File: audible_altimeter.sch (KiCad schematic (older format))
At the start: 0 parts

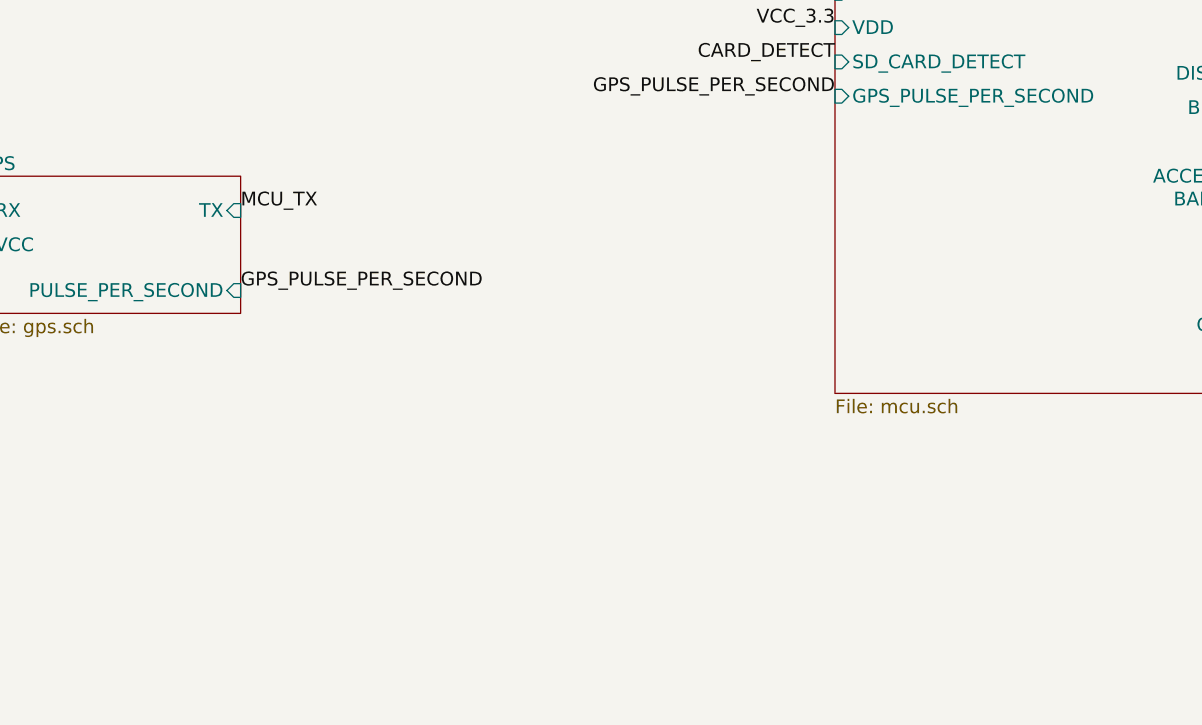
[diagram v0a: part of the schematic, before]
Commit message: Add buttons. Fix DRC. Add antenna
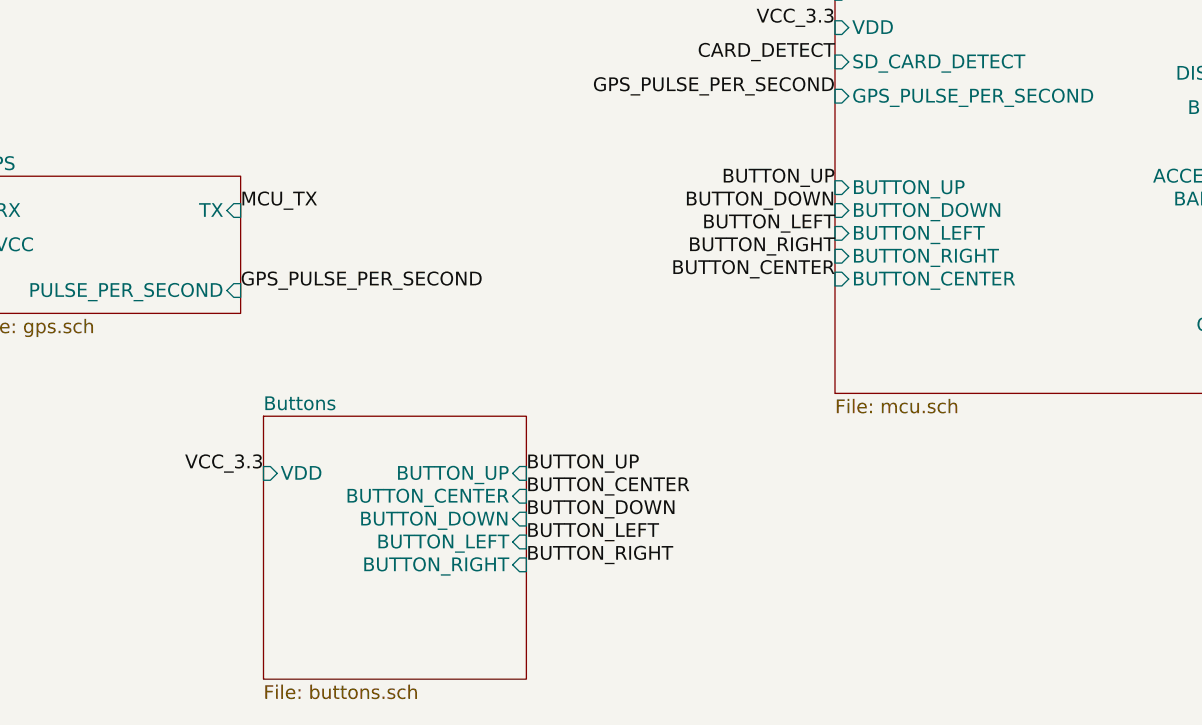
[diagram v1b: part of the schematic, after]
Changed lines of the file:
@@
 $Descr A4 11693 8268
 encoding utf-8
-Sheet 1 13
+Sheet 1 14
 Title ""
 Date ""
@@
 F21 "SD_CARD_DETECT" I L 6100 4900 60
 F22 "GPS_PULSE_PER_SECOND" I L 6100 5050 60
+F23 "BUTTON_UP" I L 6100 5450 60
+F24 "BUTTON_DOWN" I L 6100 5550 60
+F25 "BUTTON_LEFT" I L 6100 5650 60
+F26 "BUTTON_RIGHT" I L 6100 5750 60
+F27 "BUTTON_CENTER" I L 6100 5850 60
 $EndSheet
 $Sheet
@@
 Text Label 7600 1550 2    60   ~ 0
 VCC_3.3
+$Sheet
+S 3600 6450 1150 1150
+U 5463ABA7
+F0 "Buttons" 60
+F1 "buttons.sch" 60
+F2 "VDD" I L 3600 6700 60
+F3 "BUTTON_UP" I R 4750 6700 60
+F4 "BUTTON_CENTER" I R 4750 6800 60
+F5 "BUTTON_DOWN" I R 4750 6900 60
+F6 "BUTTON_LEFT" I R 4750 7000 60
+F7 "BUTTON_RIGHT" I R 4750 7100 60
+$EndSheet
+Text Label 3600 6700 2    60   ~ 0
+VCC_3.3
+Text Label 4750 6700 0    60   ~ 0
+BUTTON_UP
+Text Label 4750 6800 0    60   ~ 0
+BUTTON_CENTER
+Text Label 4750 6900 0    60   ~ 0
+BUTTON_DOWN
+Text Label 4750 7000 0    60   ~ 0
+BUTTON_LEFT
+Text Label 4750 7100 0    60   ~ 0
+BUTTON_RIGHT
+Text Label 6100 5450 2    60   ~ 0
+BUTTON_UP
+Text Label 6100 5850 2    60   ~ 0
+BUTTON_CENTER
+Text Label 6100 5550 2    60   ~ 0
+BUTTON_DOWN
+Text Label 6100 5650 2    60   ~ 0
+BUTTON_LEFT
+Text Label 6100 5750 2    60   ~ 0
+BUTTON_RIGHT
 $EndSCHEMATC

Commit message: Layouting
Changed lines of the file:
@@
 $EndSheet
 $Sheet
-S 2400 3950 1000 550
+S 1000 4000 1000 550
 U 5446183C
 F0 "Battery" 60
 F1 "batter.sch" 60
-F2 "BATTERY" I L 2400 4100 60
-F3 "+5V" I L 2400 4250 60
-F4 "+3.3V" I R 3400 4100 60
+F2 "BATTERY" I L 1000 4150 60
+F3 "+5V" I L 1000 4300 60
+F4 "+3.3V" I R 2000 4150 60
 $EndSheet
 $Sheet
@@
 $EndSheet
 $Sheet
-S 4850 3150 1100 550
+S 3450 3250 1100 550
 U 54463294
 F0 "USB" 60
 F1 "usb.sch" 60
-F2 "VBUS" I L 4850 3250 60
-F3 "D-" I L 4850 3350 60
-F4 "D+" I L 4850 3450 60
+F2 "VBUS" I L 3450 3350 60
+F3 "D-" I L 3450 3450 60
+F4 "D+" I L 3450 3550 60
 $EndSheet
 $Sheet
@@
 $EndSheet
 $Sheet
-S 7250 3000 1050 550
+S 1050 3100 1050 550
 U 54464246
 F0 "Buzzer" 60
 F1 "buzzer.sch" 60
-F2 "BATTERY" I L 7250 3200 60
-F3 "BUZZER_DRIVE" I L 7250 3350 60
+F2 "BATTERY" I L 1050 3300 60
+F3 "BUZZER_DRIVE" I L 1050 3450 60
 $EndSheet
 $Sheet
@@
 $EndSheet
 $Sheet
-S 2350 5400 1150 600
+S 950  5000 1150 600
 U 5461699E
 F0 "GPS" 60
 F1 "gps.sch" 60
-F2 "TX" I R 3500 5550 60
-F3 "RX" I L 2350 5550 60
-F4 "VCC" I L 2350 5700 60
-F5 "PULSE_PER_SECOND" I R 3500 5900 60
+F2 "TX" I R 2100 5150 60
+F3 "RX" I L 950 5150 60
+F4 "VCC" I L 950 5300 60
+F5 "PULSE_PER_SECOND" I R 2100 5500 60
 $EndSheet
 $Sheet
@@
 Text Label 3350 2000 0    60   ~ 0
 I2C_SDA
-Text Label 3400 4100 0    60   ~ 0
+Text Label 2000 4150 0    60   ~ 0
 VCC_3.3
 Text Label 2300 1900 2    60   ~ 0
@@
 Text Label 6100 4600 2    60   ~ 0
 MCU_RX
-Text Label 2350 5550 2    60   ~ 0
+Text Label 950  5150 2    60   ~ 0
 MCU_RX
-Text Label 3500 5550 0    60   ~ 0
+Text Label 2100 5150 0    60   ~ 0
 MCU_TX
-Text Label 2350 5700 2    60   ~ 0
+Text Label 950  5300 2    60   ~ 0
 VCC_3.3
 Text Label 8350 4200 0    60   ~ 0
@@
 Text Label 6100 4300 2    60   ~ 0
 D+
-Text Label 4850 3350 2    60   ~ 0
+Text Label 3450 3450 2    60   ~ 0
 D-
-Text Label 4850 3450 2    60   ~ 0
+Text Label 3450 3550 2    60   ~ 0
 D+
-Text Label 4850 3250 2    60   ~ 0
+Text Label 3450 3350 2    60   ~ 0
 +5V
-Text Label 2400 4250 2    60   ~ 0
+Text Label 1000 4300 2    60   ~ 0
 +5V
-Text Label 2400 4100 2    60   ~ 0
+Text Label 1000 4150 2    60   ~ 0
 BATTERY
-Text Label 7250 3200 2    60   ~ 0
+Text Label 1050 3300 2    60   ~ 0
 BATTERY
 Text Label 6100 4750 2    60   ~ 0
@@
 Text Label 8350 4650 0    60   ~ 0
 I2C_SDA
-Text Label 7250 3350 2    60   ~ 0
+Text Label 1050 3450 2    60   ~ 0
 BUZZER_DRIVE
 Text Label 8350 5100 0    60   ~ 0
@@
 CARD_DETECT
 NoConn ~ 3350 2200
-Text Label 3500 5900 0    60   ~ 0
+Text Label 2100 5500 0    60   ~ 0
 GPS_PULSE_PER_SECOND
 Text Label 6100 5050 2    60   ~ 0

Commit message: Start planning test board v2.0
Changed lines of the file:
@@
 $Descr A4 11693 8268
 encoding utf-8
-Sheet 1 14
+Sheet 1 10
 Title ""
 Date ""
@@
 $EndSheet
 $Sheet
-S 9600 750  1100 1150
-U 54462395
-F0 "MicroSD" 60
-F1 "micro_sd.sch" 60
-F2 "VDD" I L 9600 1050 60
-F3 "SCK" I L 9600 1200 60
-F4 "MISO" I R 10700 1050 60
-F5 "MOSI" I L 9600 1350 60
-F6 "CSn" I L 9600 1500 60
-F7 "CARD_DETECT" I R 10700 1200 60
-$EndSheet
-$Sheet
 S 2300 1750 1050 550
 U 54462AE3
@@
 F5 "DISP_ON" I L 7600 1250 60
 F6 "VDD" I L 7600 1350 60
-F7 "INVERSION_SIG" I L 7600 1450 60
-F8 "INVERSION_PROG" I L 7600 1550 60
 $EndSheet
 $Sheet
@@
 F5 "MISO" I L 6100 4450 60
 F6 "SCK" I R 8350 4350 60
-F7 "RX" I L 6100 4600 60
-F8 "TX" I R 8350 4500 60
-F9 "I2C_SDA" I R 8350 4650 60
-F10 "I2C_SCL" I R 8350 4800 60
-F11 "VDD" I L 6100 4750 60
-F12 "DISPLAY_INVERT" I R 8350 4950 60
-F13 "BUZZER_DRIVE" I R 8350 5100 60
-F14 "CLOCK_INT" I R 8350 5250 60
-F15 "ACCELERATOR_INT" I R 8350 5400 60
-F16 "BAROMETER_INT" I R 8350 5500 60
-F17 "CSn_FLASH" I R 8350 5750 60
-F18 "CSn_RAM" I R 8350 5850 60
-F19 "CSp_DISPLAY" I R 8350 5950 60
-F20 "CSn_SD_CARD" I R 8350 6050 60
-F21 "SD_CARD_DETECT" I L 6100 4900 60
-F22 "GPS_PULSE_PER_SECOND" I L 6100 5050 60
-F23 "BUTTON_UP" I L 6100 5450 60
-F24 "BUTTON_DOWN" I L 6100 5550 60
-F25 "BUTTON_LEFT" I L 6100 5650 60
-F26 "BUTTON_RIGHT" I L 6100 5750 60
-F27 "BUTTON_CENTER" I L 6100 5850 60
-$EndSheet
-$Sheet
-S 4200 750  1050 550
-U 544655FD
-F0 "9-Axis" 60
-F1 "9axis.sch" 60
-F2 "VDD" I L 4200 950 60
-F3 "I2C_SDA" I R 5250 850 60
-F4 "I2C_SCL" I R 5250 1000 60
-F5 "INT" I R 5250 1150 60
-$EndSheet
-$Sheet
-S 950  5000 1150 600
-U 5461699E
-F0 "GPS" 60
-F1 "gps.sch" 60
-F2 "TX" I R 2100 5150 60
-F3 "RX" I L 950 5150 60
-F4 "VCC" I L 950 5300 60
-F5 "PULSE_PER_SECOND" I R 2100 5500 60
-$EndSheet
-$Sheet
-S 4300 1650 1200 650
-U 5461BBD1
-F0 "Humidity" 60
-F1 "humidity.sch" 60
-F2 "I2C_SDA" I R 5500 1850 60
-F3 "VDD" I L 4300 1850 60
-F4 "I2C_SCL" I R 5500 2000 60
+F7 "I2C_SDA" I R 8350 4650 60
+F8 "I2C_SCL" I R 8350 4800 60
+F9 "VDD" I L 6100 4750 60
+F10 "BUZZER_DRIVE" I R 8350 5100 60
+F11 "CLOCK_INT" I R 8350 5250 60
+F12 "BAROMETER_INT" I R 8350 5500 60
+F13 "CSn_FLASH" I R 8350 5750 60
+F14 "CSp_DISPLAY" I R 8350 5950 60
+F15 "BUTTON_UP" I L 6100 5450 60
+F16 "BUTTON_DOWN" I L 6100 5550 60
+F17 "BUTTON_CENTER" I L 6100 5850 60
+F18 "DISP_ON" I R 8350 4950 60
 $EndSheet
 Text Label 3350 950  0    60   ~ 0
@@
 Text Label 3350 1900 0    60   ~ 0
 I2C_SCL
-Text Label 5250 1000 0    60   ~ 0
-I2C_SCL
-Text Label 5500 2000 0    60   ~ 0
-I2C_SCL
-Text Label 5500 1850 0    60   ~ 0
-I2C_SDA
-Text Label 5250 850  0    60   ~ 0
-I2C_SDA
 Text Label 3350 1050 0    60   ~ 0
 I2C_SDA
@@
 Text Label 2350 950  2    60   ~ 0
 VCC_3.3
-Text Label 4200 950  2    60   ~ 0
-VCC_3.3
-Text Label 4300 1850 2    60   ~ 0
-VCC_3.3
 Text Label 7600 1350 2    60   ~ 0
 VCC_3.3
 Text Label 7600 950  2    60   ~ 0
 SCK
-Text Label 9600 1050 2    60   ~ 0
-VCC_3.3
-Text Label 9600 1200 2    60   ~ 0
-SCK
-Text Label 9600 1350 2    60   ~ 0
-MOSI
-Text Label 9600 1500 2    60   ~ 0
-CSn_MICROSD
 Text Label 7600 1150 2    60   ~ 0
 CSp_DISPLAY
 Text Label 7600 1050 2    60   ~ 0
 MOSI
-Text Label 10700 1050 0    60   ~ 0
-MISO
-Text Label 8350 4500 0    60   ~ 0
-MCU_TX
-Text Label 6100 4600 2    60   ~ 0
-MCU_RX
-Text Label 950  5150 2    60   ~ 0
-MCU_RX
-Text Label 2100 5150 0    60   ~ 0
-MCU_TX
-Text Label 950  5300 2    60   ~ 0
-VCC_3.3
 Text Label 8350 4200 0    60   ~ 0
 MOSI
@@
 Text Label 8350 5100 0    60   ~ 0
 BUZZER_DRIVE
-Text Label 8350 4950 0    60   ~ 0
-DISPLAY_INVERT
-Text Label 7600 1450 2    60   ~ 0
-DISPLAY_INVERT
 Text Label 8350 5250 0    60   ~ 0
 CLOCK_INT
@@
 Text Label 8350 5500 0    60   ~ 0
 BAROMETER_INT
-Text Label 8350 5400 0    60   ~ 0
-ACCELERATOR_INT
-Text Label 5250 1150 0    60   ~ 0
-ACCELERATOR_INT
 $Sheet
 S 9550 2250 1350 1000
@@
 F3 "MOSI" I L 9550 2600 60
 F4 "MISO" I R 10900 2600 60
-F5 "CSn_RAM" I L 9550 2750 60
-F6 "CSn_FLASH" I L 9550 2900 60
-F7 "VDD" I L 9550 3050 60
+F5 "CSn_FLASH" I L 9550 2900 60
+F6 "VDD" I L 9550 3050 60
 $EndSheet
 Text Label 9550 2450 2    60   ~ 0
@@
 Text Label 9550 2600 2    60   ~ 0
 MOSI
-Text Label 9550 2750 2    60   ~ 0
-CSn_RAM
 Text Label 9550 2900 2    60   ~ 0
 CSn_FLASH
@@
 Text Label 10900 2600 0    60   ~ 0
 MISO
-Text Label 8350 6050 0    60   ~ 0
-CSn_MICROSD
 Text Label 8350 5950 0    60   ~ 0
 CSp_DISPLAY
-Text Label 8350 5850 0    60   ~ 0
-CSn_RAM
 Text Label 8350 5750 0    60   ~ 0
 CSn_FLASH
-Text Label 10700 1200 0    60   ~ 0
-CARD_DETECT
-Text Label 6100 4900 2    60   ~ 0
-CARD_DETECT
 NoConn ~ 3350 2200
-Text Label 2100 5500 0    60   ~ 0
-GPS_PULSE_PER_SECOND
-Text Label 6100 5050 2    60   ~ 0
-GPS_PULSE_PER_SECOND
-Text Label 7600 1550 2    60   ~ 0
-VCC_3.3
 $Sheet
 S 3600 6450 1150 1150
@@
 F0 "Buttons" 60
 F1 "buttons.sch" 60
-F2 "VDD" I L 3600 6700 60
-F3 "BUTTON_UP" I R 4750 6700 60
-F4 "BUTTON_CENTER" I R 4750 6800 60
-F5 "BUTTON_DOWN" I R 4750 6900 60
-F6 "BUTTON_LEFT" I R 4750 7000 60
-F7 "BUTTON_RIGHT" I R 4750 7100 60
-$EndSheet
-Text Label 3600 6700 2    60   ~ 0
-VCC_3.3
+F2 "BUTTON_UP" I R 4750 6700 60
+F3 "BUTTON_CENTER" I R 4750 6800 60
+F4 "BUTTON_DOWN" I R 4750 6900 60
+$EndSheet
 Text Label 4750 6700 0    60   ~ 0
 BUTTON_UP
@@
 Text Label 4750 6900 0    60   ~ 0
 BUTTON_DOWN
-Text Label 4750 7000 0    60   ~ 0
-BUTTON_LEFT
-Text Label 4750 7100 0    60   ~ 0
-BUTTON_RIGHT
 Text Label 6100 5450 2    60   ~ 0
 BUTTON_UP
@@
 Text Label 6100 5550 2    60   ~ 0
 BUTTON_DOWN
-Text Label 6100 5650 2    60   ~ 0
-BUTTON_LEFT
-Text Label 6100 5750 2    60   ~ 0
-BUTTON_RIGHT
+Text Label 8350 4950 0    60   ~ 0
+DISP_ON
+Text Label 7600 1250 2    60   ~ 0
+DISP_ON
 $EndSCHEMATC

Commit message: Start implementing new version: move USB port and altimeter module, new buzzer and volume control
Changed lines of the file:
@@
 F2 "BATTERY" I L 1050 3300 60
 F3 "BUZZER_DRIVE" I L 1050 3450 60
+F4 "3.3V" I R 2100 3250 60
+F5 "SCL" I R 2100 3350 60
+F6 "SDA" I R 2100 3450 60
 $EndSheet
 $Sheet
@@
 Text Label 7600 1250 2    60   ~ 0
 DISP_ON
+Text Label 2100 3250 0    60   ~ 0
+VCC_3.3
+Text Label 2100 3450 0    60   ~ 0
+I2C_SDA
+Text Label 2100 3350 0    60   ~ 0
+I2C_SCL
 $EndSCHEMATC

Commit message: Before starting laying out tracks
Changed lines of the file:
@@
 $Descr A4 11693 8268
 encoding utf-8
-Sheet 1 10
+Sheet 1 11
 Title ""
 Date ""
@@
 F17 "BUTTON_CENTER" I L 6100 5850 60
 F18 "DISP_ON" I R 8350 4950 60
+F19 "ACC_INT" I L 6100 5100 60
 $EndSheet
 Text Label 3350 950  0    60   ~ 0
@@
 Text Label 2100 3350 0    60   ~ 0
 I2C_SCL
+$Sheet
+S 1050 5300 1250 600
+U 553028FD
+F0 "Accelerometer" 60
+F1 "accelerometer.sch" 60
+F2 "VDD" I L 1050 5450 60
+F3 "I2C_SDA" I R 2300 5500 60
+F4 "I2C_SCL" I R 2300 5600 60
+F5 "INT" I R 2300 5700 60
+$EndSheet
+Text Label 1050 5450 2    60   ~ 0
+VCC_3.3
+Text Label 2300 5600 0    60   ~ 0
+I2C_SCL
+Text Label 2300 5500 0    60   ~ 0
+I2C_SDA
+Text Label 2300 5700 0    60   ~ 0
+ACC_INT
+Text Label 6100 5100 2    60   ~ 0
+ACC_INT
 $EndSCHEMATC

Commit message: Some changes?
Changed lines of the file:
@@
 $Descr A4 11693 8268
 encoding utf-8
-Sheet 1 11
+Sheet 1 10
 Title ""
 Date ""
@@
 F3 "+5V" I L 1000 4300 60
 F4 "+3.3V" I R 2000 4150 60
+F5 "BATTERY_SENSE" I R 2000 4450 60
 $EndSheet
 $Sheet
@@
 F17 "BUTTON_CENTER" I L 6100 5850 60
 F18 "DISP_ON" I R 8350 4950 60
-F19 "ACC_INT" I L 6100 5100 60
+F19 "BATTERY_SENSE" I L 6100 5100 60
 $EndSheet
 Text Label 3350 950  0    60   ~ 0
@@
 Text Label 2100 3350 0    60   ~ 0
 I2C_SCL
-$Sheet
-S 1050 5300 1250 600
-U 553028FD
-F0 "Accelerometer" 60
-F1 "accelerometer.sch" 60
-F2 "VDD" I L 1050 5450 60
-F3 "I2C_SDA" I R 2300 5500 60
-F4 "I2C_SCL" I R 2300 5600 60
-F5 "INT" I R 2300 5700 60
-$EndSheet
-Text Label 1050 5450 2    60   ~ 0
-VCC_3.3
-Text Label 2300 5600 0    60   ~ 0
-I2C_SCL
-Text Label 2300 5500 0    60   ~ 0
-I2C_SDA
-Text Label 2300 5700 0    60   ~ 0
-ACC_INT
+Text Label 2000 4450 0    60   ~ 0
+BATTERY_SENSE
 Text Label 6100 5100 2    60   ~ 0
-ACC_INT
+BATTERY_SENSE
 $EndSCHEMATC
